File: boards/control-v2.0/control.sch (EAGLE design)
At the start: 103 parts, among them IC1 MCP23017-E/SS, J1 HFW8R-1ST, J2 B2PS-CENTERED-VH(LF)(SN), J3 SBH11-PBPC-D05-RA, J9 DF22-2, U1 TLV70233DBVR, U3 VND5E006ASPTR-E, U4 LMZ14201, U5 MCP1824T-1202E/OT, U6 MCP1824T-2502E/OT, X1 ASV-18.432MHZ-EJ-T

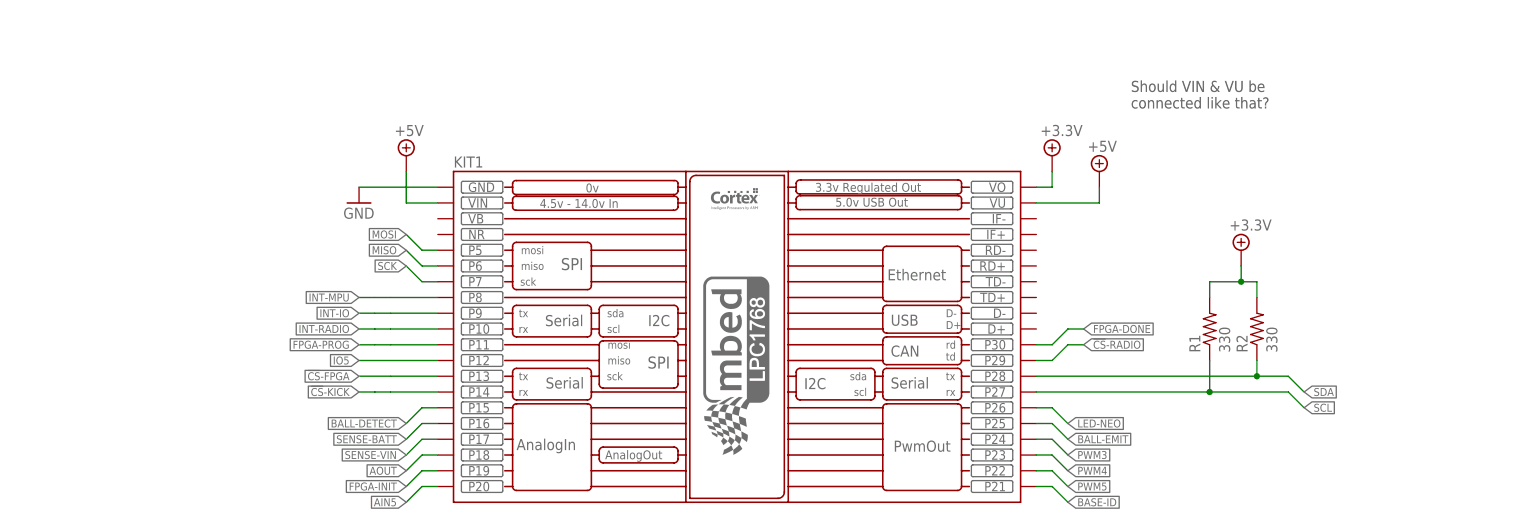
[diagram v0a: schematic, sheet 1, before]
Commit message: More control board routing, mostly motors
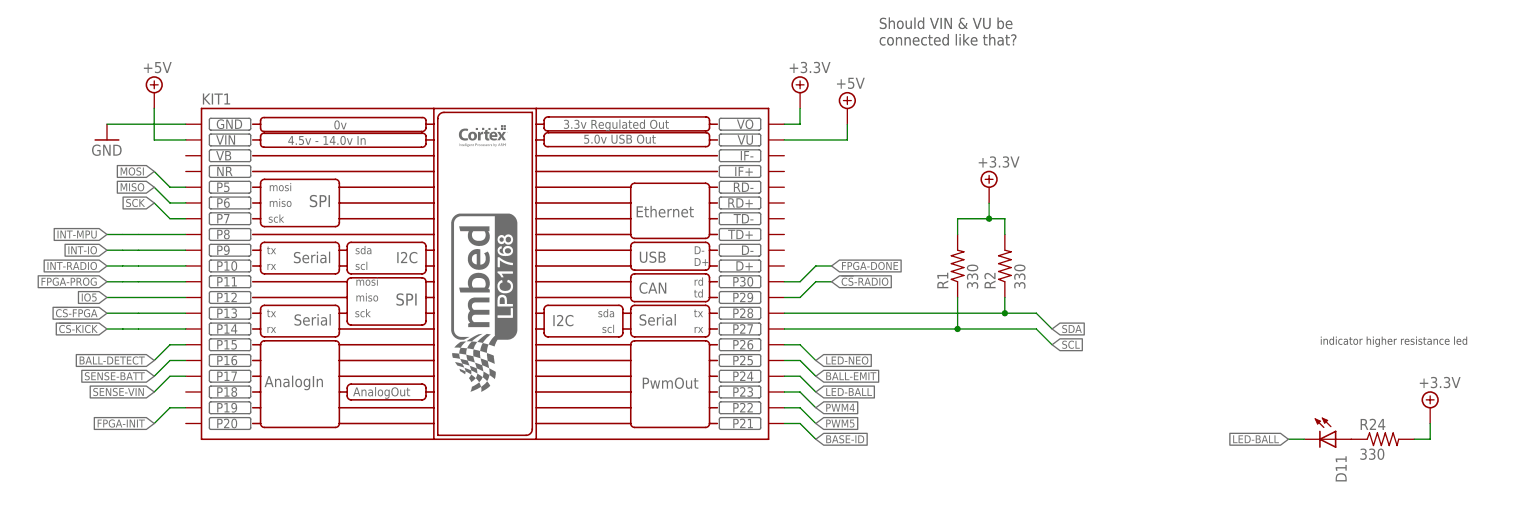
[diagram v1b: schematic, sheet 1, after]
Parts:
- removed R14: 100k, rcl:R-US_R0603
- added D11: (no value), RoboJackets-LEDs:LED_SMD
- added D12, D13: GREEN, RoboJackets-LEDs:LED_SMD
- added R24, R25: 330, resistor:R-US_R0603
- added SB1, SB2, SB3, SB4: (no value), RoboJackets-Switches:SOLDERBRIDGESB0603
- D4, D5: value RED -> GREEN
- R13: value 270k -> 1k; device rcl:R-US_R0603 -> resistor:R-US_R0603
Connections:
- removed net AIN5: KIT1.P20
- removed net AOUT: KIT1.P18
- removed net N$11: IC1.GPB6, RN1.7
- removed net N$73: S1G$1.COMMON, U3.IN1, U3.IN2
- removed net N$76: R13.2, R14.2, U4.EN
- removed net N$81: D4.K, R17.2
- removed net N$82: D5.K, R18.2
- removed net N$9: IC1.GPB4, RN1.5
- removed net PWM3: KIT1.P24
- new net +1.2V-PRE: SB2.1, U5.V_OUT
- new net +2.5V-PRE: SB3.1, U6.V_OUT
- new net +3.3V-PRE: SB1.1, U1.VOUT
- new net EN-PWR: S1G$1.COMMON, U3.IN1, U3.IN2, U4.EN
- new net LED-BALL: D11.K, KIT1.P24
- new net N$33: D11.A, R24.1
- new net N$34: D4.A, R17.2
- new net N$36: D5.A, R18.2
- new net N$38: D12.A, R25.1
- new net N$39: D13.A, R13.2
- new net N$40: F2.2, SB4.1
- new net N$5: IC1.GPB4, RN1.4
- net +1.2V: now also SB2.2; no longer U5.V_OUT
- net +18.5V: no longer C7.1, R12.1, R13.1, U4.VIN
- net +2.5V: now also SB3.2; no longer U6.V_OUT
- net +3.3V: now also R24.2, R25.2, SB1.2; no longer D4.A, D5.A, U1.VOUT
- net +5V: now also R13.1, SB4.2; no longer F2.2
- net GND: now also D12.K, D13.K, D4.K, D5.K; no longer R14.1, U1.SN1, U1.SN2, U1.SP1, U1.SP2
- net LED-DD1: now also RN1.12; no longer RN1.13
- net LED-MPU: now also RN1.15; no longer RN1.10
- net LED-RADIO: now also RN1.11; no longer RN1.14
- net LED-SENSE: now also RN1.13; no longer RN1.12
- net LED-WD1: now also RN1.10; no longer RN1.15
- net LED-WD2: now also RN1.9; no longer RN1.16
- net LED-WD3: now also RN1.14; no longer RN1.11
- net LED-WD4: now also RN1.16; no longer RN1.9
- net N$1: now also RN1.8; no longer RN1.1
- net N$10: no longer IC1.GPB5, RN1.6
- net N$12: no longer IC1.GPB7, RN1.8
- net N$2: now also IC1.GPB1, RN1.7
- net N$3: now also IC1.GPB2, RN1.6
- net N$4: now also IC1.GPB3, RN1.5
- net N$6: now also IC1.GPB5, RN1.3; no longer IC1.GPB1, RN1.2
- net N$7: now also IC1.GPB6, RN1.2; no longer IC1.GPB2, RN1.3
- net N$8: now also IC1.GPB7, RN1.1; no longer IC1.GPB3, RN1.4
- net PHASE-A: now also C7.2, U1.SH_B
- net PHASE-B: now also C6.2, U1.SH_A
- net R-P60: now also U$1.31_IO/VREF_3; no longer U$1.31_IP/VREF_3
- net VBATT: now also C7.1, R12.1, U4.VIN
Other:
- note added: "indicator higher resistance led"
- note removed: "Add jumpers to 1.2 & 2.5?"
- note removed: "Do we need indicator LED on 1.2 & 2.4?"
- moved on the sheet: D5, KIT1, R1, R13, R17, R2, R22, R3, RN1, U1, U5, U6

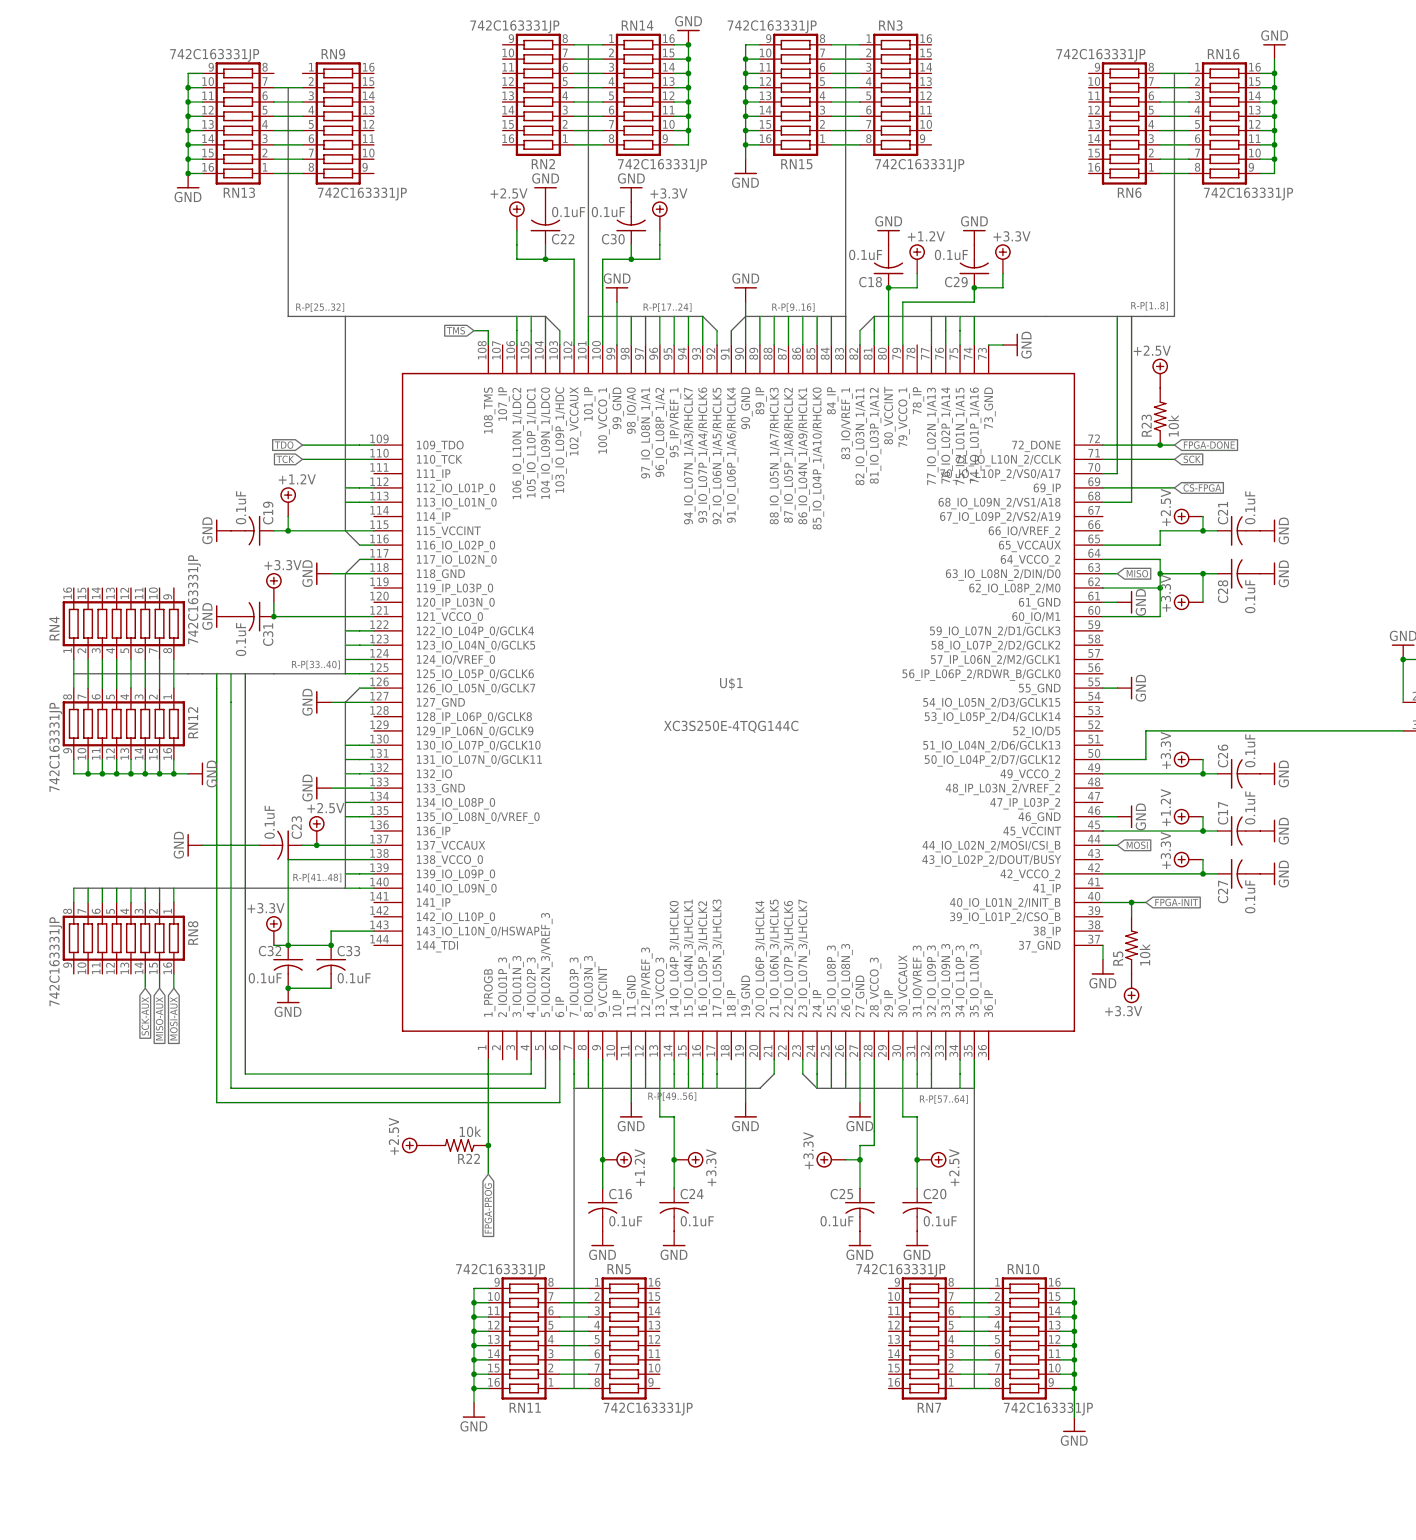
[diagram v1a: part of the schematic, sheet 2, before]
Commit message: Most control board routing done, still messy
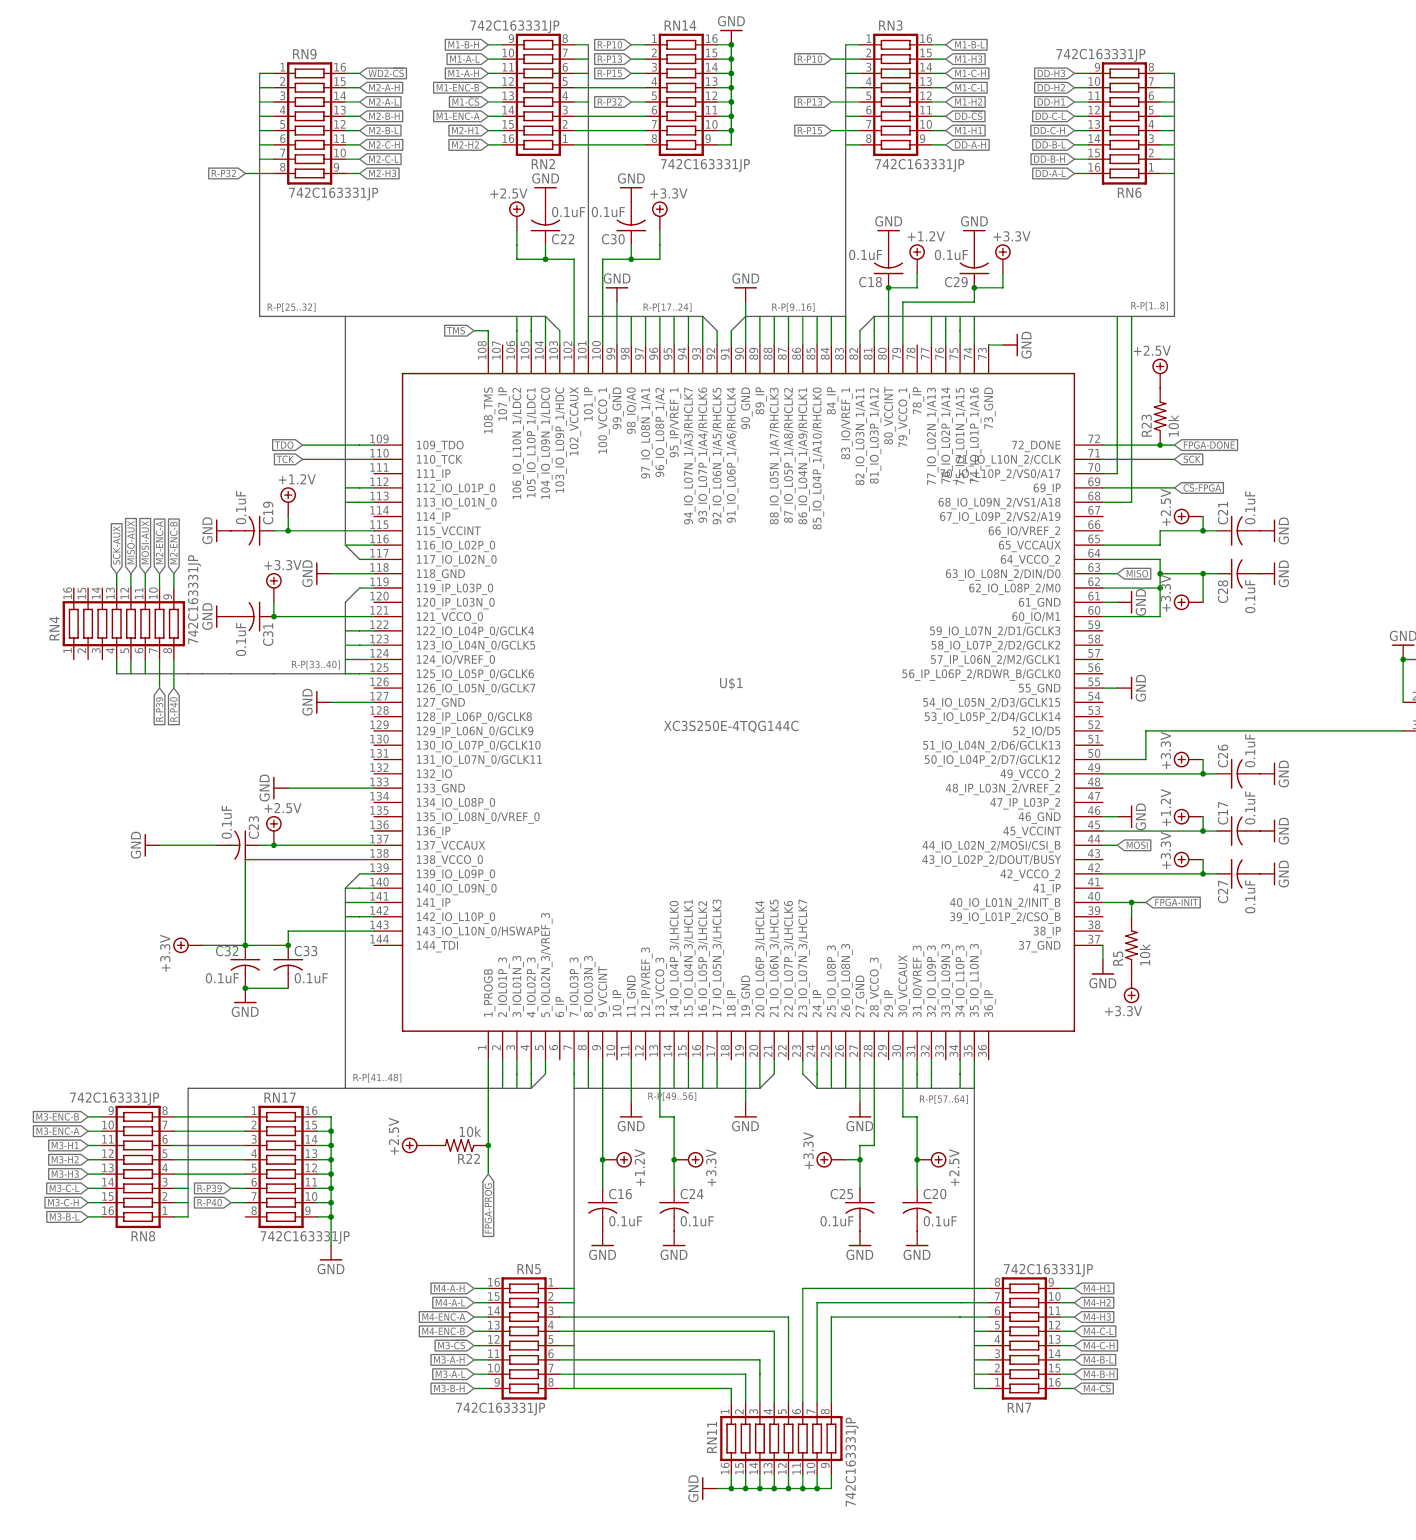
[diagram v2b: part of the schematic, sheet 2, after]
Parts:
- removed RN10, RN12, RN13, RN15, RN16: 742C163331JP, RoboJackets-Resistors:742C163331JP
- added RN17: 742C163331JP, RoboJackets-Resistors:742C163331JP
- D11: value (none) -> BLUE
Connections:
- removed net !RST: J1G$1.4, J3.5
- removed net INTA: IC1.INTA
- removed net LED-DD1: D2.K, RN1.12
- removed net LED-SENSE: RN1.13
- removed net LED-WD1: D1.K, RN1.10
- removed net LED-WD2: D8.K, RN1.9
- removed net LED-WD3: D7.K, RN1.14
- removed net LED-WD4: D6.K, RN1.16
- removed net R-P33: RN12.8, RN4.1, U$1.6_IP
- removed net R-P34: RN12.7, RN4.2, U$1.5_IOL02N_3/VREF_3
- removed net R-P35: RN12.6, RN4.3, U$1.4_IOL02P_3
- new net !RST!-KICK: J1G$1.4
- new net !RST!-RADIO: J3.5
- new net DD-!CS: RN3.11
- new net DD-A-H: RN3.9
- new net DD-A-L: RN6.16
- new net DD-B-H: RN6.15
- new net DD-B-L: RN6.14
- new net DD-C-H: RN6.13
- new net DD-C-L: RN6.12
- new net DD-H1: RN6.11
- new net DD-H2: RN6.10
- new net DD-H3: RN6.9
- new net LED-DD: D2.K, RN1.16
- new net LED-M1: D1.K, RN1.15
- new net LED-M2: D8.K, RN1.14
- new net LED-M3: D7.K, RN1.12
- new net LED-M4: D6.K, RN1.13
- new net LED-SOMETHING: RN1.9
- new net M1-!CS: RN2.13
- new net M1-A-H: RN2.11
- new net M1-A-L: RN2.10
- new net M1-B-H: RN2.9
- new net M1-B-L: RN3.16
- new net M1-C-H: RN3.14
- new net M1-C-L: RN3.13
- new net M1-ENC-A: RN2.14
- new net M1-ENC-B: RN2.12
- new net M1-H1: RN3.10
- new net M1-H2: RN3.12
- new net M1-H3: RN3.15
- new net M2-A-H: RN9.15
- new net M2-A-L: RN9.14
- new net M2-B-H: RN9.13
- new net M2-B-L: RN9.12
- new net M2-C-H: RN9.11
- new net M2-C-L: RN9.10
- new net M2-ENC-A: RN4.10
- new net M2-ENC-B: RN4.9
- new net M2-H1: RN2.15
- new net M2-H2: RN2.16
- new net M2-H3: RN9.9
- new net M3-!CS: RN5.12
- new net M3-A-H: RN5.11
- new net M3-A-L: RN5.10
- new net M3-B-H: RN5.9
- new net M3-B-L: RN8.16
- new net M3-C-H: RN8.15
- new net M3-C-L: RN8.14
- new net M3-ENC-A: RN8.10
- new net M3-ENC-B: RN8.9
- new net M3-H1: RN8.11
- new net M3-H2: RN8.12
- new net M3-H3: RN8.13
- new net M4-!CS: RN7.16
- new net M4-A-H: RN5.16
- new net M4-A-L: RN5.15
- new net M4-B-H: RN7.15
- new net M4-B-L: RN7.14
- new net M4-C-H: RN7.13
- new net M4-C-L: RN7.12
- new net M4-ENC-A: RN5.14
- new net M4-ENC-B: RN5.13
- new net M4-H1: RN7.9
- new net M4-H2: RN7.10
- new net M4-H3: RN7.11
- new net R-P25: RN9.1, U$1.117_IO_L02N_0
- new net WD2-!CS: RN9.16
- net GND: now also RN17.10, RN17.11, RN17.12, RN17.13, RN17.14, RN17.15, RN17.16, RN17.9; no longer RN10.10, RN10.11, RN10.12, RN10.13, RN10.14, RN10.15, RN10.16, RN10.9, RN12.10, RN12.11, RN12.12, RN12.13, RN12.14, RN12.15, RN12.16, RN12.9, RN13.10, RN13.11, RN13.12, RN13.13, RN13.14, RN13.15, RN13.16, RN13.9, RN15.10, RN15.11, RN15.12, RN15.13, RN15.14, RN15.15, RN15.16, RN15.9, RN16.10, RN16.11, RN16.12, RN16.13, RN16.14, RN16.15, RN16.16, RN16.9
- net HEX-2: now also IC1.GPA5; no longer IC1.GPA7
- net HEX-3: now also IC1.GPA7; no longer IC1.GPA5
- net INT-IO: now also IC1.INTA
- net LED-MPU: now also RN1.10; no longer RN1.15
- net MISO-AUX: now also RN4.12; no longer RN8.15
- net MOSI-AUX: now also RN4.11; no longer RN8.16
- net R-P1: no longer RN16.8
- net R-P10: now also RN14.1; no longer RN15.7
- net R-P11: no longer RN15.6
- net R-P12: no longer RN15.5
- net R-P13: now also RN14.2; no longer RN15.4
- net R-P14: no longer RN15.3
- net R-P15: now also RN14.3; no longer RN15.2
- net R-P16: no longer RN15.1
- net R-P2: no longer RN16.7
- net R-P20: no longer RN14.5
- net R-P22: no longer RN14.3
- net R-P23: no longer RN14.2
- net R-P24: no longer RN14.1
- net R-P26: no longer RN13.7
- net R-P27: no longer RN13.6
- net R-P28: no longer RN13.5
- net R-P29: no longer RN13.4
- net R-P3: no longer RN16.6
- net R-P30: no longer RN13.3
- net R-P31: no longer RN13.2
- net R-P32: now also RN14.5; no longer RN13.1
- net R-P36: no longer RN12.5
- net R-P37: no longer RN12.4
- net R-P38: no longer RN12.3
- net R-P39: now also RN17.6; no longer RN12.2
- net R-P4: no longer RN16.5
- net R-P40: now also RN17.7, U$1.119_IP_L03P_0; no longer RN12.1, U$1.117_IO_L02N_0
- net R-P41: now also U$1.5_IOL02N_3/VREF_3; no longer U$1.140_IO_L09N_0
- net R-P42: now also U$1.4_IOL02P_3; no longer U$1.139_IO_L09P_0
- net R-P43: now also U$1.3_IOL01N_3; no longer U$1.135_IO_L08N_0/VREF_0
- net R-P44: now also RN17.5, U$1.2_IOL01P_3; no longer U$1.134_IO_L08P_0
- net R-P45: now also RN17.4, U$1.142_IO_L10P_0; no longer U$1.132_IO
- net R-P46: now also RN17.3, U$1.141_IP; no longer U$1.131_IO_L07N_0/GCLK11
- net R-P47: now also RN17.2, U$1.140_IO_L09N_0; no longer U$1.130_IO_L07P_0/GCLK10
- net R-P48: now also RN17.1, U$1.139_IO_L09P_0; no longer U$1.126_IO_L05N_0/GCLK7
- net R-P49: no longer RN11.8
- net R-P5: no longer RN16.4
- net R-P50: now also U$1.20_IO_L06P_3/LHCLK4; no longer RN11.7, U$1.17_IO_L05N_3/LHCLK3
- net R-P51: now also RN11.5, U$1.17_IO_L05N_3/LHCLK3; no longer RN11.6, U$1.16_IO_L05P_3/LHCLK2
- net R-P52: now also RN11.4, U$1.16_IO_L05P_3/LHCLK2; no longer RN11.5, U$1.15_IO_L04N_3/LHCLK1
- net R-P53: now also U$1.15_IO_L04N_3/LHCLK1; no longer RN11.4, U$1.14_IO_L04P_3/LHCLK0
- net R-P54: now also U$1.14_IO_L04P_3/LHCLK0; no longer U$1.12_IP/VREF_3
- net R-P57: no longer RN10.8
- net R-P58: no longer RN10.7
- net R-P59: no longer RN10.6
- net R-P6: no longer RN16.3
- net R-P60: no longer RN10.5
- net R-P61: no longer RN10.4
- net R-P62: now also RN11.8; no longer RN10.3
- net R-P63: now also RN11.7; no longer RN10.2
- net R-P64: now also RN11.6; no longer RN10.1
- net R-P7: no longer RN16.2
- net R-P8: no longer RN16.1
- net R-P9: no longer RN15.8
- net SCK-AUX: now also RN4.13; no longer RN8.14
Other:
- moved on the sheet: C23, C32, C33, RN11, RN14, RN5, RN7, RN8, RN9
